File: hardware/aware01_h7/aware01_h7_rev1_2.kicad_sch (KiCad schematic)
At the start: 60 parts, among them J1 Conn_01x06_Pin, J2 Conn_01x03_Pin, SW1 SW_Push, U1 STM32H7B0ZBTx, U2 IS45S16800F-7TLA2, Y1 WE-XTAL 24.0MHz 50ppm

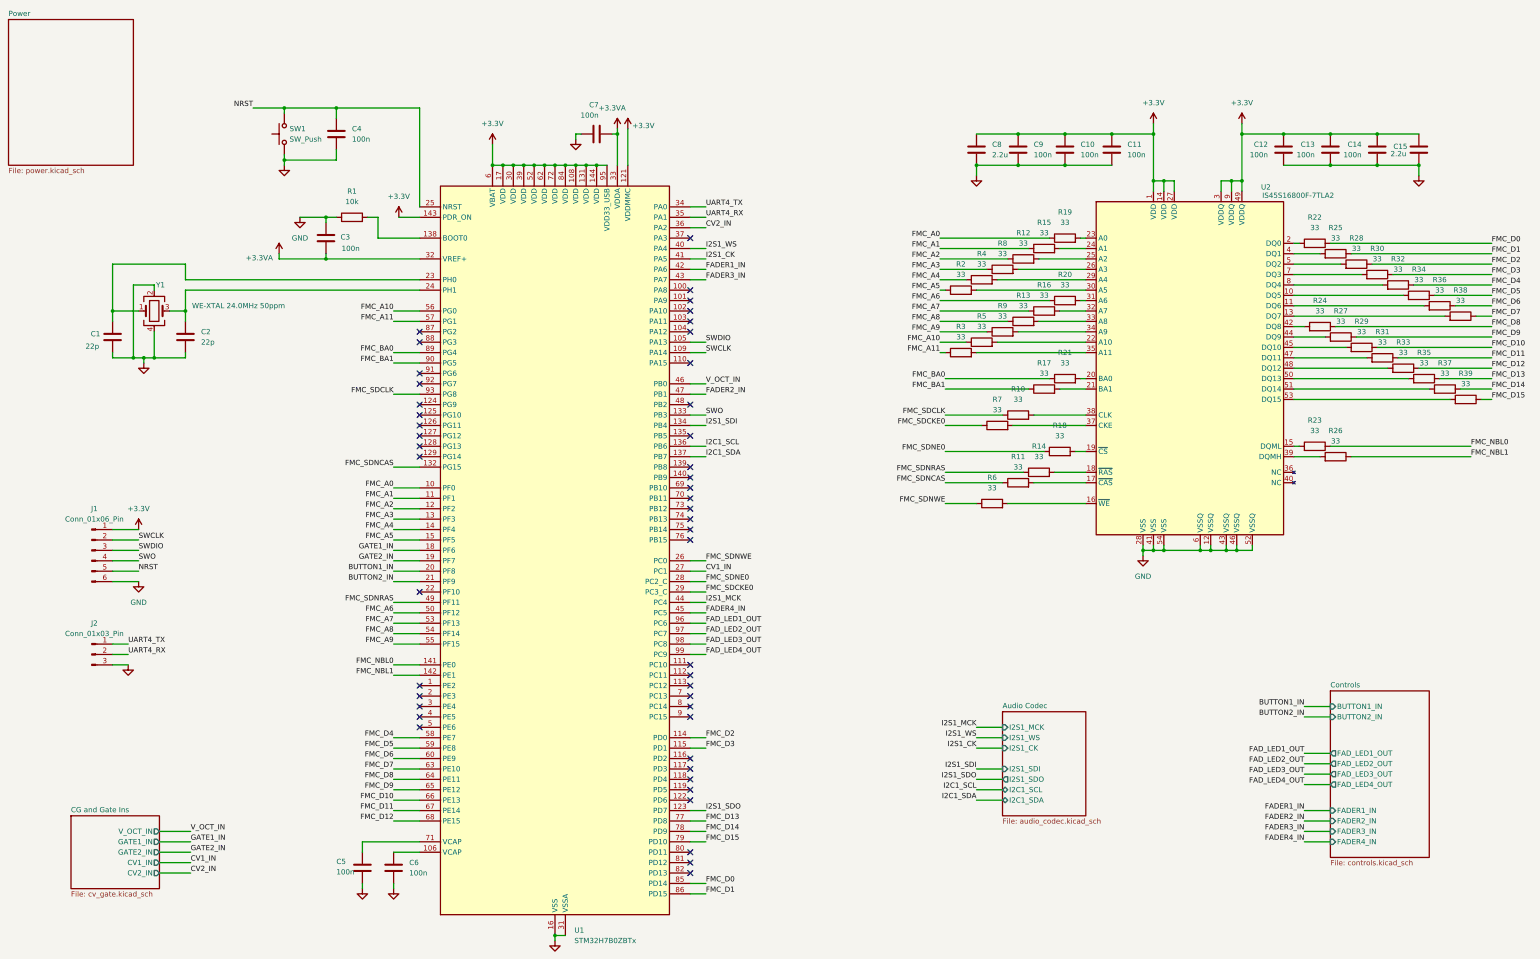
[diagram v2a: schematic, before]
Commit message: add 3rd Gate In and add resistor part No's
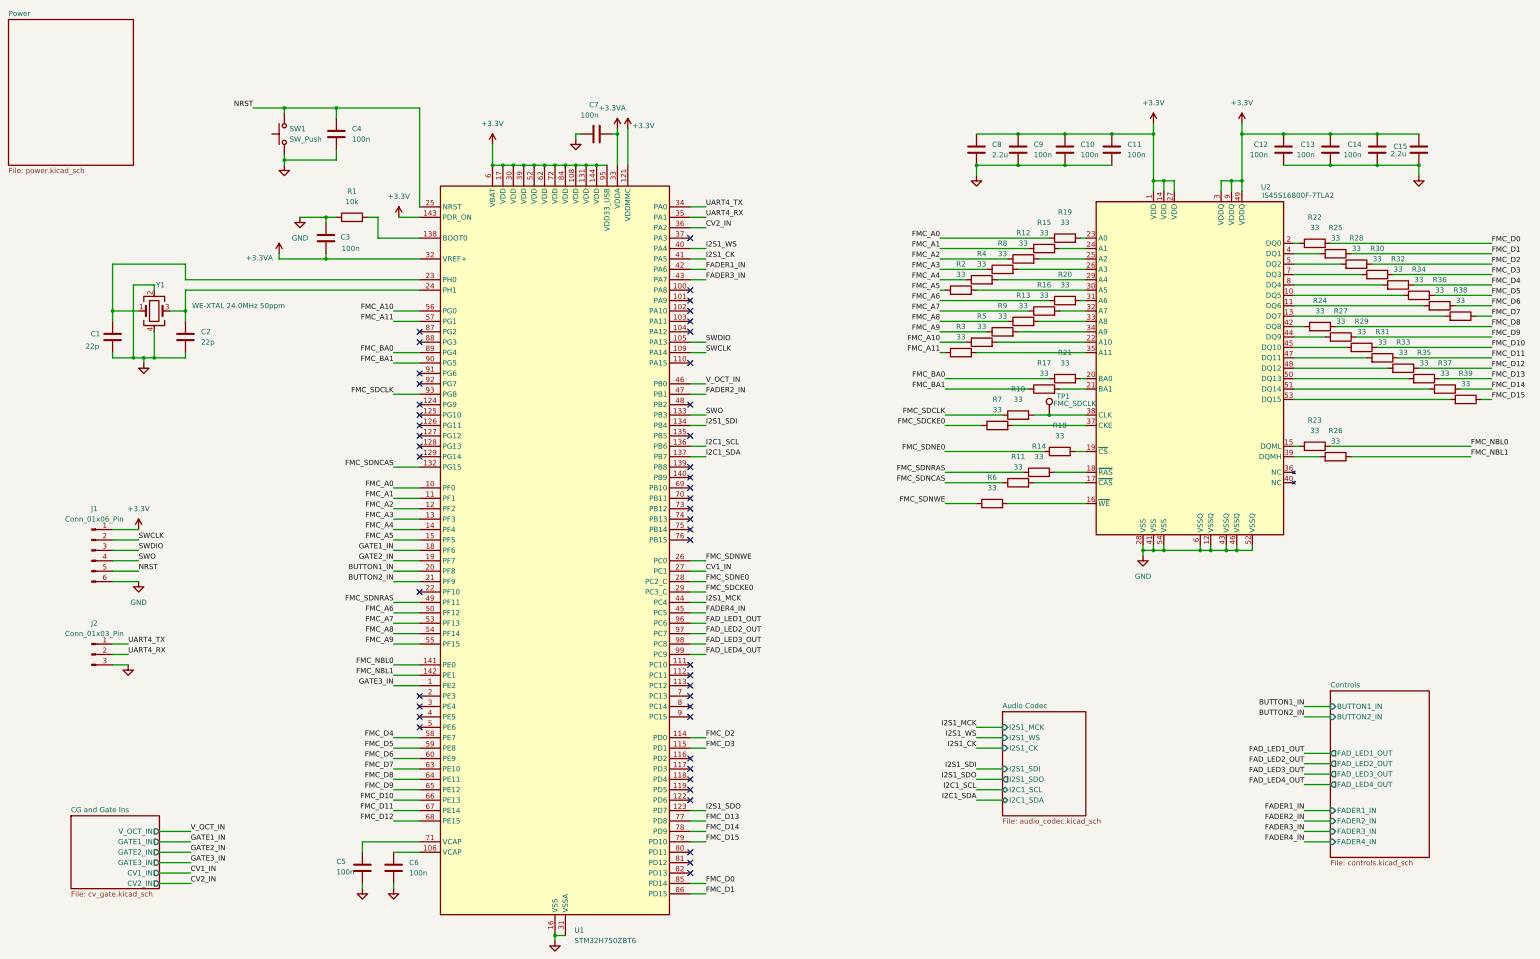
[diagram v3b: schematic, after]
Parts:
- added TP1: FMC_SDCLK, TestPoint:TestPoint_Pad_1.0x1.0mm, symbol Connector:TestPoint
- R1: Manufacturer_Name (none) -> Welwyn Components / TT Electronics; Manufacturer_Part_Number (none) -> WCR0603-10KFA; Mouser Part Number (none) -> 756-WCR0603-10KFA
- U1: value STM32H7B0ZBTx -> STM32H750ZBT6; Manufacturer_Part_Number STM32H7B0ZBT6 -> STM32H750ZBT6; Mouser Part Number 511-STM32H7B0ZBT6 -> 511-STM32H750ZBT6
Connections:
- net at R10.2, U2.38 (CLK): now also TP1.1
- net GATE3_IN: now reaches U1.1 (PE2)
- no-connect marks 47 -> 46
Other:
- sheet CG and Gate Ins ports: added GATE3_IN; removed none
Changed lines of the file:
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@@
 	)
 	(junction
+		(at 283.21 124.46)
+		(diameter 0)
+		(color 0 0 0 0)
+	)
+	(junction
 		(at 265.43 63.5)
 		(diameter 0)
@@
 	)
 	(no_connect
-		(at 129.54 190.5)
-	)
-	(no_connect
 		(at 129.54 195.58)
 	)
@@
 	(wire
 		(pts
-			(xy 279.4 124.46) (xy 292.1 124.46)
+			(xy 279.4 124.46) (xy 283.21 124.46)
 		)
 		(stroke
@@
 	(wire
 		(pts
+			(xy 66.04 233.68) (xy 73.66 233.68)
+		)
+		(stroke
+			(width 0)
+			(type default)
+		)
+	)
+	(wire
+		(pts
 			(xy 265.43 205.74) (xy 271.78 205.74)
 		)
@@
 	(wire
 		(pts
-			(xy 66.04 233.68) (xy 73.66 233.68)
+			(xy 66.04 236.22) (xy 73.66 236.22)
 		)
 		(stroke
@@
 	(wire
 		(pts
-			(xy 66.04 236.22) (xy 73.66 236.22)
+			(xy 66.04 238.76) (xy 73.66 238.76)
 		)
 		(stroke
@@
 	(wire
 		(pts
+			(xy 283.21 124.46) (xy 292.1 124.46)
+		)
+		(stroke
+			(width 0)
+			(type default)
+		)
+	)
+	(wire
+		(pts
 			(xy 257.81 118.11) (xy 278.13 118.11)
 		)
@@
 	(wire
 		(pts
+			(xy 123.19 190.5) (xy 129.54 190.5)
+		)
+		(stroke
+			(width 0)
+			(type default)
+		)
+	)
+	(wire
+		(pts
 			(xy 368.3 110.49) (xy 391.16 110.49)
 		)
@@
 	)
 	(label "CV2_IN"
-		(at 73.66 236.22 0)
+		(at 73.66 238.76 0)
 		(effects
 			(font
@@
 		)
 	)
+	(label "GATE3_IN"
+		(at 123.19 190.5 180)
+		(effects
+			(font
+				(size 1.27 1.27)
+			)
+			(justify right bottom)
+		)
+	)
 	(label "FMC_A2"
 		(at 123.19 147.32 180)
@@
 		)
 	)
+	(label "GATE3_IN"
+		(at 73.66 233.68 0)
+		(effects
+			(font
+				(size 1.27 1.27)
+			)
+			(justify left bottom)
+		)
+	)
 	(label "FMC_SDNE0"
 		(at 257.81 133.35 180)
@@
 	)
 	(label "CV1_IN"
-		(at 73.66 233.68 0)
+		(at 73.66 236.22 0)
 		(effects
 			(font
@@
 	)
 	(symbol
+		(lib_id "Connector:TestPoint")
+		(at 283.21 124.46 0)
+		(unit 1)
+		(exclude_from_sim no)
+		(in_bom yes)
+		(on_board yes)
+		(dnp no)
+		(property "Reference" "TP1"
+			(at 284.988 119.888 0)
+			(effects
+				(font
+					(size 1.27 1.27)
+				)
+				(justify left)
+			)
+		)
+		(property "Value" "FMC_SDCLK"
+			(at 284.226 121.666 0)
+			(effects
+				(font
+					(size 1.27 1.27)
+				)
+				(justify left)
+			)
+		)
+		(property "Footprint" "TestPoint:TestPoint_Pad_1.0x1.0mm"
+			(at 288.29 124.46 0)
+			(effects
+				(font
+					(size 1.27 1.27)
+				)
+				(hide yes)
+			)
+		)
+		(property "Datasheet" "~"
+			(at 288.29 124.46 0)
+			(effects
+				(font
+					(size 1.27 1.27)
+				)
+				(hide yes)
+			)
+		)
+		(property "Description" "test point"
+			(at 283.21 124.46 0)
+			(effects
+				(font
+					(size 1.27 1.27)
+				)
+				(hide yes)
+			)
+		)
+		(pin "1"
+		)
+		(instances
+			(project ""
+				(path "/efd43d7c-3c18-45dd-8fa5-4bf32165850f"
+					(reference "TP1")
+					(unit 1)
+				)
+			)
+		)
+	)
+	(symbol
 		(lib_id "Device:R")
 		(at 276.86 86.36 90)
@@
 			)
 		)
-		(property "Value" "STM32H7B0ZBTx"
+		(property "Value" "STM32H750ZBT6"
 			(at 167.2941 252.73 0)
 			(effects
@@
 			)
 		)
-		(property "Datasheet" "https://www.st.com/resource/en/datasheet/stm32h7b0zb.pdf"
+		(property "Datasheet" "https://www.mouser.de/datasheet/2/389/stm32h750ib-1761001.pdf"
 			(at 162.56 157.48 0)
 			(effects
@@
 			)
 		)
-		(property "Manufacturer_Part_Number" "STM32H7B0ZBT6"
+		(property "Manufacturer_Part_Number" "STM32H750ZBT6"
 			(at 162.56 157.48 0)
 			(effects
@@
 			)
 		)
-		(property "Mouser Part Number" " 511-STM32H7B0ZBT6"
+		(property "Mouser Part Number" "511-STM32H750ZBT6"
 			(at 162.56 157.48 0)
 			(effects
@@
 			)
 		)
+		(property "Manufacturer_Name" "Welwyn Components / TT Electronics"
+			(at 113.03 76.2 0)
+			(effects
+				(font
+					(size 1.27 1.27)
+				)
+				(hide yes)
+			)
+		)
+		(property "Manufacturer_Part_Number" "WCR0603-10KFA"
+			(at 113.03 76.2 0)
+			(effects
+				(font
+					(size 1.27 1.27)
+				)
+				(hide yes)
+			)
+		)
+		(property "Mouser Part Number" "756-WCR0603-10KFA"
+			(at 113.03 76.2 0)
+			(effects
+				(font
+					(size 1.27 1.27)
+				)
+				(hide yes)
+			)
+		)
 		(pin "2"
 		)
@@
 		)
 		(pin "CV1_IN" output
-			(at 66.04 233.68 0)
+			(at 66.04 236.22 0)
 			(effects
 				(font
@@
 		)
 		(pin "CV2_IN" output
-			(at 66.04 236.22 0)
+			(at 66.04 238.76 0)
+			(effects
+				(font
+					(size 1.27 1.27)
+				)
+				(justify right)
+			)
+		)
+		(pin "GATE3_IN" output
+			(at 66.04 233.68 0)
 			(effects
 				(font

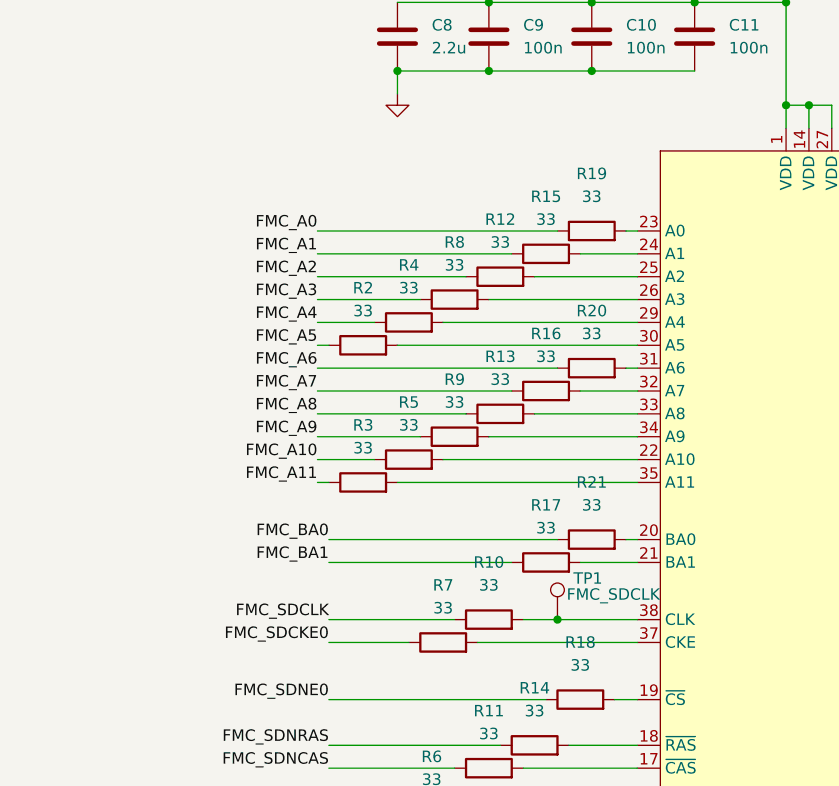
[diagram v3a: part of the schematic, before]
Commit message: slight changes to layout
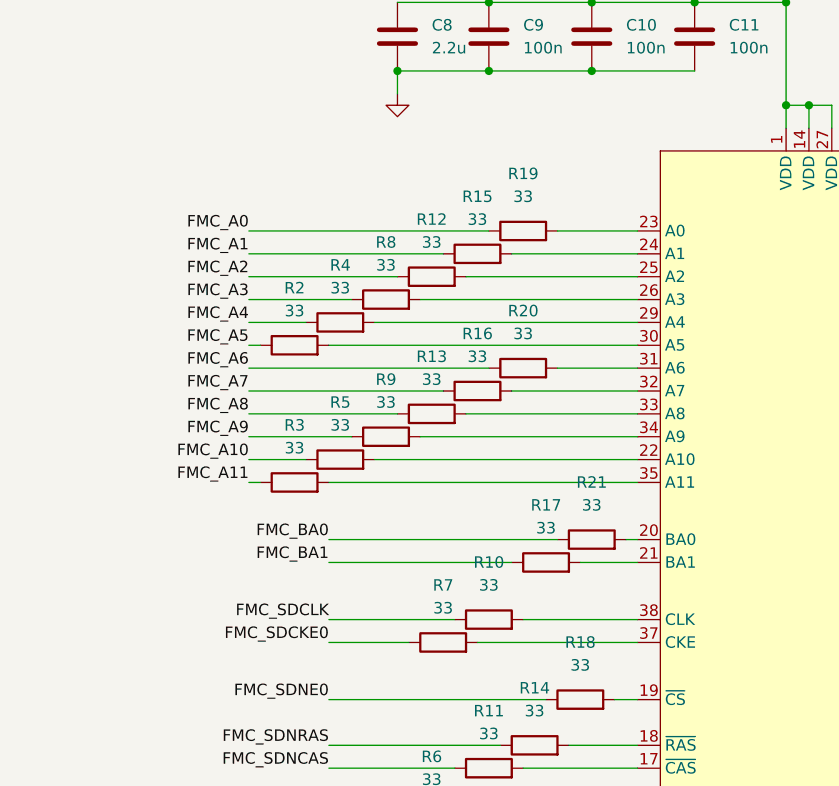
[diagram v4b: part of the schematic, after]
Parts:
- removed TP1: FMC_SDCLK, TestPoint:TestPoint_Pad_1.0x1.0mm, symbol Connector:TestPoint
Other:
- moved on the sheet: R12, R13, R15, R16, R19, R2, R20, R3, R4, R5, R8, R9
